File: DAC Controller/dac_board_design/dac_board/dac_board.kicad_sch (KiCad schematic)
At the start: 12 parts

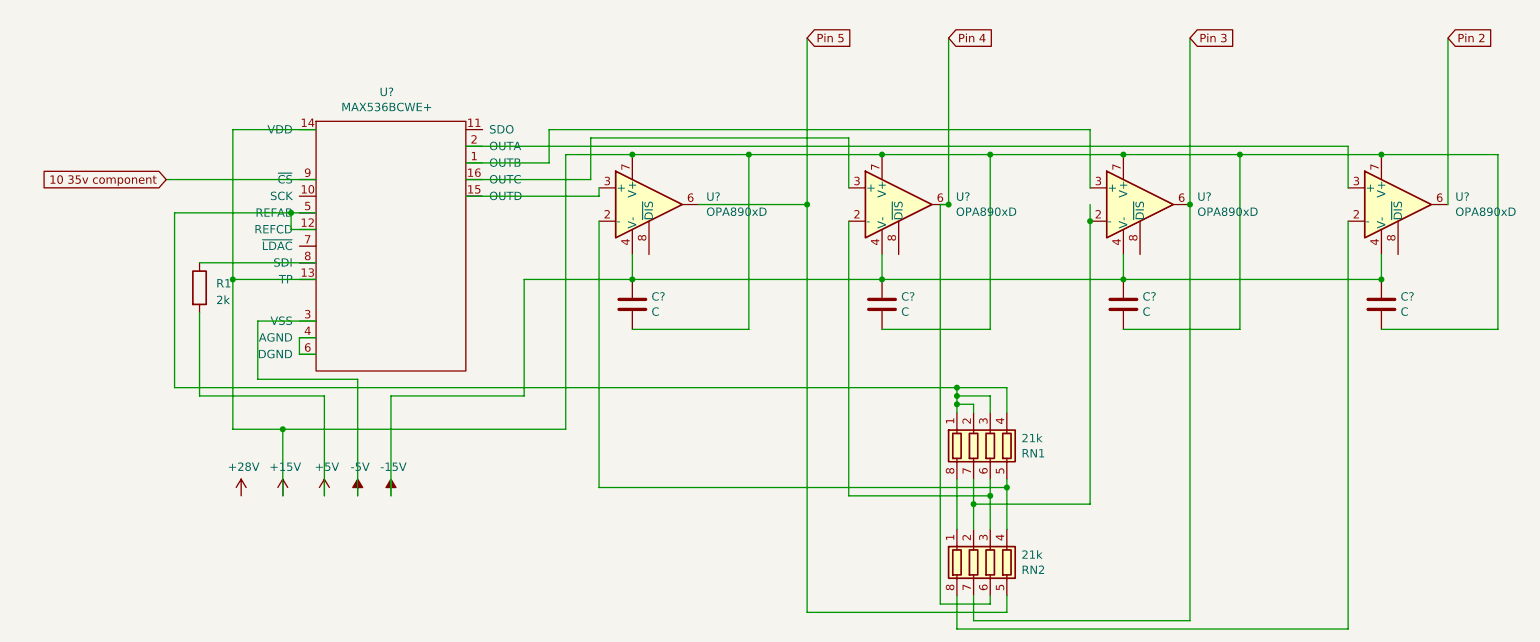
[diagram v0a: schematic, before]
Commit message: Reorganize Schematic
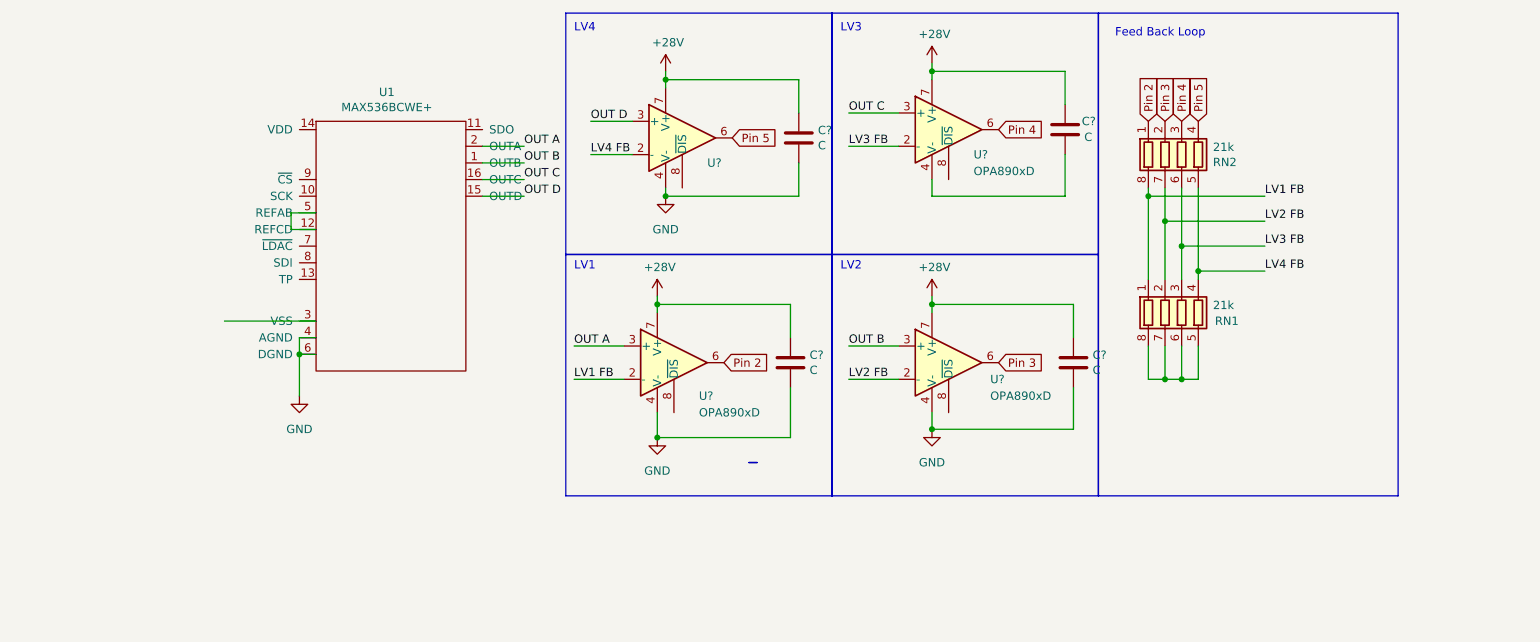
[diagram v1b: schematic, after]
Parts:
- removed R1: 2k, symbol Device:R
- gave numbers to parts that had none: 1
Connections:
- net +28V: now also C?.1, C?.1, C?.1, C?.1, U?.7 (V+), U?.7 (V+), U?.7 (V+), U?.7 (V+)
- net Pin 2: now also RN2.1 (R1.1)
- net Pin 3: now also RN2.2 (R2.1); no longer RN2.7 (R2.2)
- net Pin 4: now also RN2.3 (R3.1); no longer RN2.6 (R3.2)
- net Pin 5: now also RN2.4 (R4.1); no longer RN2.5 (R4.2)
- net at U1.1 (OUTB): no longer U?.3 (+)
- net at U1.15 (OUTD): no longer U?.3 (+)
- net at U1.16 (OUTC): no longer U?.3 (+)
- net at U1.2 (OUTA): no longer U?.3 (+)
- net GND: now reaches U1.4 (AGND), U1.6 (DGND)
- net GND: now also C?.2, C?.2, C?.2, U?.4 (V-), U?.4 (V-), U?.4 (V-)
- net LV1 FB: now reaches RN2.8 (R1.2), U?.2 (-)
- net LV1 FB: now also RN1.1 (R1.1)
- net at RN1.8 (R1.2): now also RN1.5 (R4.2), RN1.6 (R3.2), RN1.7 (R2.2); no longer RN2.1 (R1.1)
- removed net +15V: C?.2, C?.2, C?.2, C?.2, U1.13 (TP), U1.14 (VDD), U?.7 (V+), U?.7 (V+), U?.7 (V+), U?.7 (V+)
- removed net -15V: C?.1, C?.1, C?.1, C?.1, U?.4 (V-), U?.4 (V-), U?.4 (V-), U?.4 (V-)
- net -5V: no longer names the net of U1.3 (VSS)
- net 10 35v component: no longer names the net of U1.9 (~{CS})
- new net: U1.12 (REFCD), U1.5 (REFAB)
- new net: C?.2, U?.4 (V-)
- new net LV2 FB: RN1.2 (R2.1), RN2.7 (R2.2), U?.2 (-)
- new net LV3 FB: RN1.3 (R3.1), RN2.6 (R3.2), U?.2 (-)
- new net LV4 FB: RN1.4 (R4.1), RN2.5 (R4.2), U?.2 (-)
- new net OUT A: U?.3 (+)
- new net OUT B: U?.3 (+)
- new net OUT C: U?.3 (+)
- new net OUT D: U?.3 (+)
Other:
- note added: "Feed Back Loop"
- note added: "LV1"
- note added: "LV2"
- note added: "LV3"
- note added: "LV4"
- moved on the sheet: C?, RN1, RN2, U?

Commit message: Move Schematic to subsheet
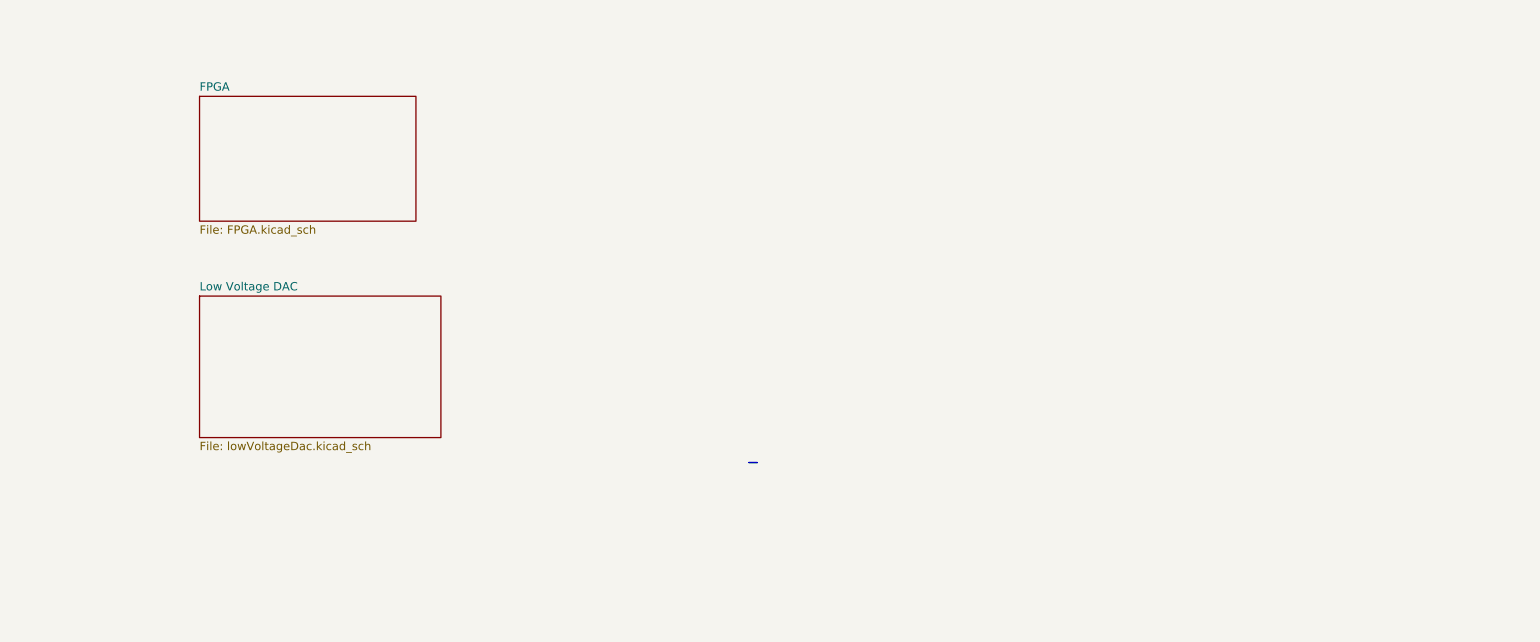
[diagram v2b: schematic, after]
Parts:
- removed C? (x4): C, symbol Device:C
- removed RN1, RN2: 21k, symbol Device:R_Pack04
- removed U1: MAX536BCWE+, symbol Created Symbols for DACBoard:MAX536BCWE+
- removed U? (x4): OPA890xD, Package_SO:SOIC-8_3.9x4.9mm_P1.27mm, symbol Amplifier_Operational:OPA890xD
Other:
- added sheet FPGA  (FPGA.kicad_sch)
- added sheet Low Voltage DAC (lowVoltageDac.kicad_sch)
- note removed: "Feed Back Loop"
- note removed: "LV1"
- note removed: "LV2"
- note removed: "LV3"
- note removed: "LV4"
